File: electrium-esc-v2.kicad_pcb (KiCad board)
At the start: 2 copper layers, 42.3 x 45.4 mm, 65 parts, among them IC1 LMR36510FADDAR, J1 CAN, J2 Conn_01x02, J3 USB_B_Micro, J4 Debugger Pins, J5 GPIO, U1 W25Q128JVS, U2 NCP1117-3.3_SOT223, U3 RP2040, U4 DRV8323HRTAR, U5 NRF24L01_Breakout, U6 SN65HVD233, Y1 ABLS-12.000MHZ-B4-T

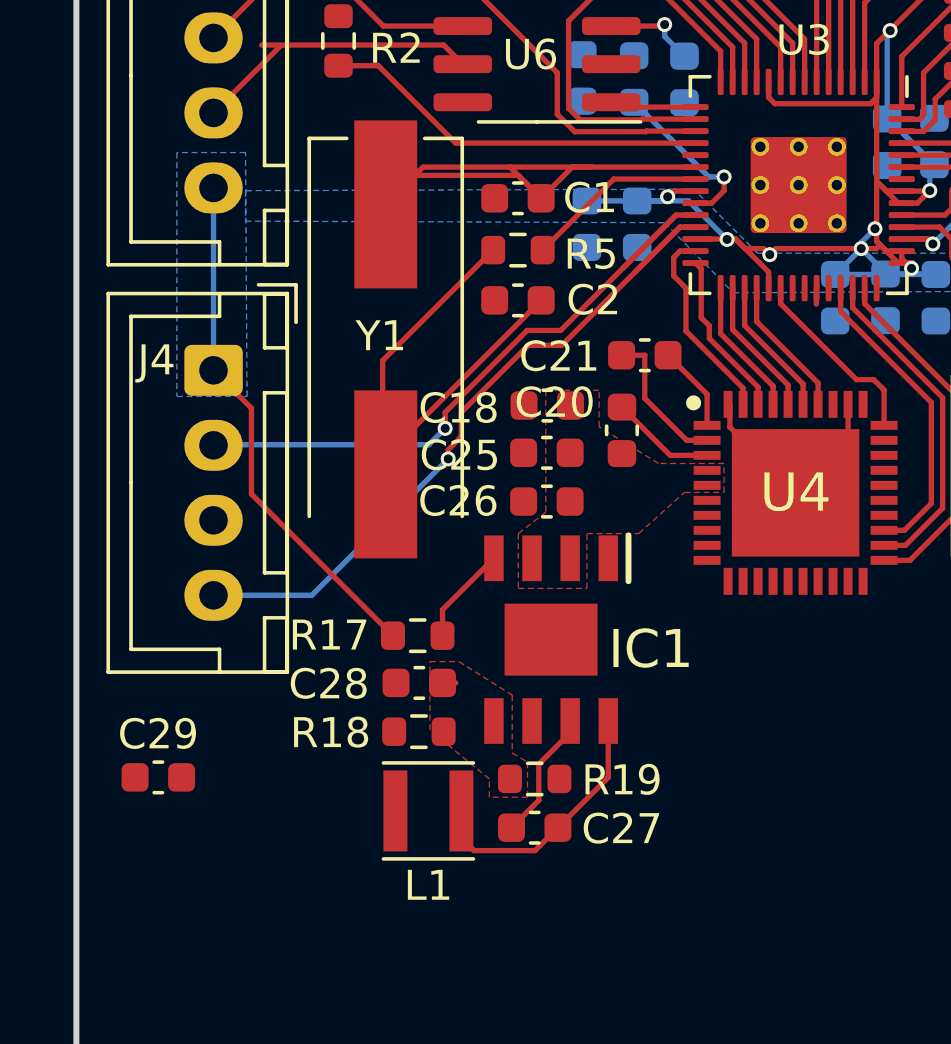
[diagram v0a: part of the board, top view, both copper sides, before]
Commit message: Add proper footprints
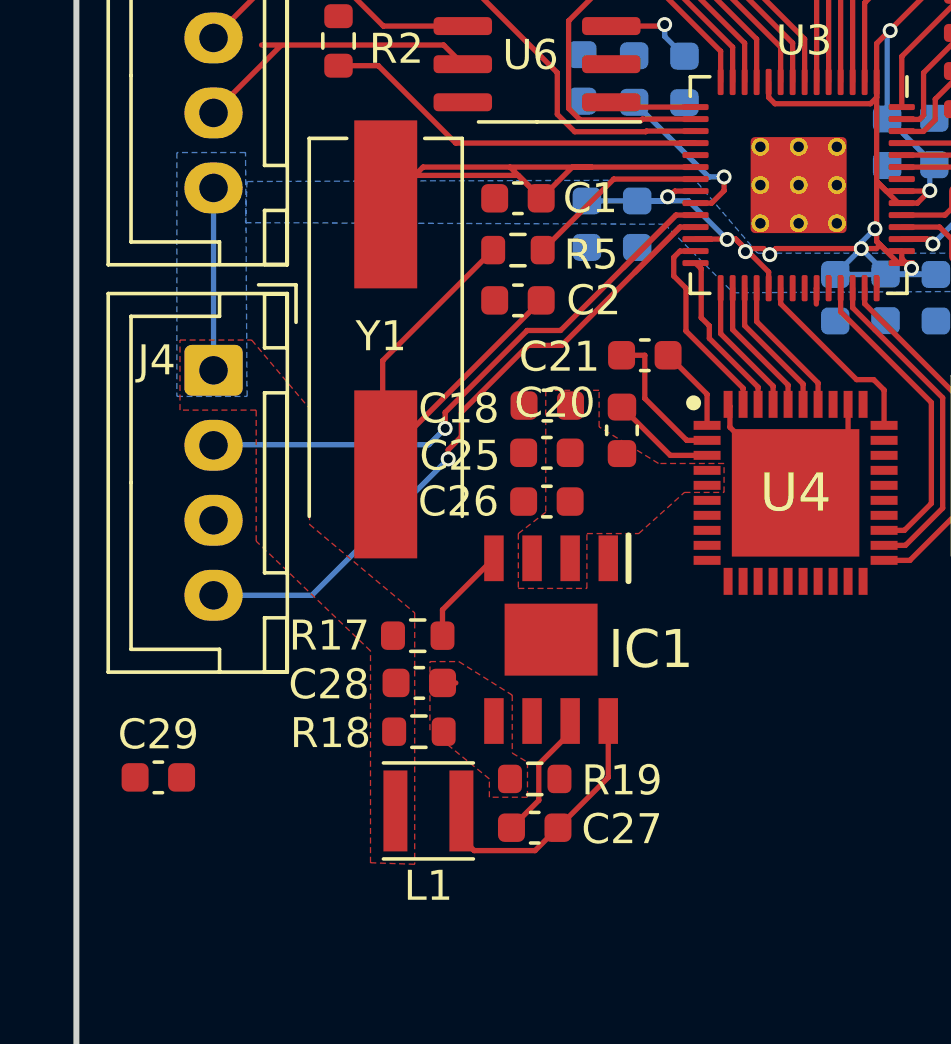
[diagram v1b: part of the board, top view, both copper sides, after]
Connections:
- R2 pad 2: /MCU (RP2040)/LED -> (no net)
- U5 pad 3: /MCU (RP2040)/NRF_CE -> (no net)
- U5 pad 4: /MCU (RP2040)/NRF_CS -> (no net)
- U5 pad 5: /MCU (RP2040)/NRF_CLK -> (no net)
- U5 pad 6: /MCU (RP2040)/NRF_MOSI -> (no net)
- U5 pad 7: /MCU (RP2040)/NRF_MISO -> (no net)
- U6 pad 1: /MCU (RP2040)/CANTX -> (no net)
- U6 pad 4: /MCU (RP2040)/CANRX -> (no net)
- U6 pad 5: /MCU (RP2040)/LBK -> (no net)
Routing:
- net +3.3V: track 105.5 -> 94.3 mm, vias 10 -> 11
- added copper zone on F.Cu, net +3.3V
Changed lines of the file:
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@@
       (net 15 "Net-(D2-A)") (pintype "passive"))
     (pad "2" smd roundrect (at 0.825 0 270) (size 0.8 0.95) (layers "F.Cu" "F.Paste" "F.Mask") (roundrect_rratio 0.25)
-      (net 33 "/MCU (RP2040)/LED") (pintype "passive"))
+      (pintype "passive"))
     (model "${KICAD6_3DMODEL_DIR}/Resistor_SMD.3dshapes/R_0603_1608Metric.wrl"
       (offset (xyz 0 0 0))
@@
       (net 5 "+3.3V") (pinfunction "VCC") (pintype "power_in"))
     (pad "3" thru_hole circle (at 0 2.54 90) (size 1.7 1.7) (drill 1) (layers "*.Cu" "*.Mask")
-      (net 53 "/MCU (RP2040)/NRF_CE") (pinfunction "CE") (pintype "input"))
+      (pinfunction "CE") (pintype "input"))
     (pad "4" thru_hole circle (at 2.54 2.54 90) (size 1.7 1.7) (drill 1) (layers "*.Cu" "*.Mask")
-      (net 50 "/MCU (RP2040)/NRF_CS") (pinfunction "~{CSN}") (pintype "input"))
+      (pinfunction "~{CSN}") (pintype "input"))
     (pad "5" thru_hole circle (at 0 5.08 90) (size 1.7 1.7) (drill 1) (layers "*.Cu" "*.Mask")
-      (net 51 "/MCU (RP2040)/NRF_CLK") (pinfunction "SCK") (pintype "input"))
+      (pinfunction "SCK") (pintype "input"))
     (pad "6" thru_hole circle (at 2.54 5.08 90) (size 1.7 1.7) (drill 1) (layers "*.Cu" "*.Mask")
-      (net 52 "/MCU (RP2040)/NRF_MOSI") (pinfunction "MOSI") (pintype "input"))
+      (pinfunction "MOSI") (pintype "input"))
     (pad "7" thru_hole circle (at 0 7.62 90) (size 1.7 1.7) (drill 1) (layers "*.Cu" "*.Mask")
-      (net 49 "/MCU (RP2040)/NRF_MISO") (pinfunction "MISO") (pintype "output"))
+      (pinfunction "MISO") (pintype "output"))
     (pad "8" thru_hole circle (at 2.54 7.62 90) (size 1.7 1.7) (drill 1) (layers "*.Cu" "*.Mask")
       (net 68 "unconnected-(U5-IRQ-Pad8)") (pinfunction "IRQ") (pintype "output+no_connect"))
@@
       (stroke (width 0.1) (type solid)) (layer "F.Fab"))
     (pad "1" smd roundrect (at -2.475 -1.905 180) (size 1.95 0.6) (layers "F.Cu" "F.Paste" "F.Mask") (roundrect_rratio 0.25)
-      (net 54 "/MCU (RP2040)/CANTX") (pinfunction "D") (pintype "input"))
+      (pinfunction "D") (pintype "input"))
     (pad "2" smd roundrect (at -2.475 -0.635 180) (size 1.95 0.6) (layers "F.Cu" "F.Paste" "F.Mask") (roundrect_rratio 0.25)
       (net 2 "GND") (pinfunction "GND") (pintype "power_in"))
@@
       (net 5 "+3.3V") (pinfunction "VCC") (pintype "power_in"))
     (pad "4" smd roundrect (at -2.475 1.905 180) (size 1.95 0.6) (layers "F.Cu" "F.Paste" "F.Mask") (roundrect_rratio 0.25)
-      (net 55 "/MCU (RP2040)/CANRX") (pinfunction "R") (pintype "output"))
+      (pinfunction "R") (pintype "output"))
     (pad "5" smd roundrect (at 2.475 1.905 180) (size 1.95 0.6) (layers "F.Cu" "F.Paste" "F.Mask") (roundrect_rratio 0.25)
-      (net 56 "/MCU (RP2040)/LBK") (pinfunction "LBK") (pintype "input"))
+      (pinfunction "LBK") (pintype "input"))
     (pad "6" smd roundrect (at 2.475 0.635 180) (size 1.95 0.6) (layers "F.Cu" "F.Paste" "F.Mask") (roundrect_rratio 0.25)
       (net 18 "/CAN/CANL") (pinfunction "CANL") (pintype "bidirectional"))
@@
   (segment (start 184.984723 60.2305) (end 184.664 59.909777) (width 0.1778) (layer "F.Cu") (net 5))
   (segment (start 194.906 51.309352) (end 192.041924 48.445276) (width 0.1778) (layer "F.Cu") (net 5))
+  (segment (start 180.2892 60.154223) (end 180.2892 60.2488) (width 0.1778) (layer "F.Cu") (net 5))
   (segment (start 184.779712 60.025488) (end 184.664 59.909777) (width 0.1778) (layer "F.Cu") (net 5))
   (segment (start 184.984723 58.2305) (end 184.664 57.909777) (width 0.1778) (layer "F.Cu") (net 5))
@@
   (segment (start 185.5015 60.2305) (end 184.984723 60.2305) (width 0.1778) (layer "F.Cu") (net 5))
   (segment (start 185.5015 58.2305) (end 184.984723 58.2305) (width 0.1778) (layer "F.Cu") (net 5))
-  (segment (start 179.965477 59.8305) (end 181.064 60.929023) (width 0.1778) (layer "F.Cu") (net 5))
+  (segment (start 179.965477 59.8305) (end 180.2892 60.154223) (width 0.1778) (layer "F.Cu") (net 5))
   (segment (start 184.15 60.1472) (end 184.2008 60.1472) (width 0.1778) (layer "F.Cu") (net 5))
   (segment (start 184.664 55.112) (end 184.664 54.593) (width 0.1778) (layer "F.Cu") (net 5))
   (segment (start 177.546 52.7304) (end 177.5968 52.7812) (width 0.1778) (layer "F.Cu") (net 5))
-  (segment (start 168.5422 73.0504) (end 163.8239 68.3321) (width 0.1778) (layer "F.Cu") (net 5))
   (segment (start 190.6016 69.444) (end 190.6016 67.9196) (width 0.1778) (layer "F.Cu") (net 5))
-  (segment (start 163.8239 68.3321) (end 163.8239 65.4697) (width 0.1778) (layer "F.Cu") (net 5))
+  (segment (start 180.2892 60.2488) (end 180.383777 60.2488) (width 0.1778) (layer "F.Cu") (net 5))
   (segment (start 180.8988 60.1472) (end 181.102 60.3504) (width 0.1778) (layer "F.Cu") (net 5))
   (segment (start 178.6265 58.2305) (end 177.9387 58.2305) (width 0.1778) (layer "F.Cu") (net 5))
   (segment (start 188.304748 44.7081) (end 181.3519 44.7081) (width 0.1778) (layer "F.Cu") (net 5))
   (segment (start 175.8188 52.7304) (end 177.546 52.7304) (width 0.1778) (layer "F.Cu") (net 5))
+  (segment (start 180.383777 60.2488) (end 181.064 60.929023) (width 0.1778) (layer "F.Cu") (net 5))
   (segment (start 184.664 59.43) (end 184.664 57.909777) (width 0.1778) (layer "F.Cu") (net 5))
   (segment (start 186.0223 58.6305) (end 186.436 58.2168) (width 0.1778) (layer "F.Cu") (net 5))
   (segment (start 190.3476 63.0932) (end 189.0587 61.8043) (width 0.1778) (layer "F.Cu") (net 5))
-  (segment (start 163.8239 65.4697) (end 162.56 64.2058) (width 0.1778) (layer "F.Cu") (net 5))
   (segment (start 181.064 55.109777) (end 181.273623 55.3194) (width 0.1778) (layer "F.Cu") (net 5))
   (segment (start 184.4566 55.3194) (end 184.664 55.112) (width 0.1778) (layer "F.Cu") (net 5))
@@
   (via (at 181.102 60.3504) (size 0.5) (drill 0.3) (layers "F.Cu" "B.Cu") (net 5))
   (via (at 185.8264 60.8076) (size 0.5) (drill 0.3) (layers "F.Cu" "B.Cu") (net 5))
+  (via (at 180.2892 60.2488) (size 0.5) (drill 0.3) (layers "F.Cu" "B.Cu") (net 5))
   (via (at 179.6796 59.8424) (size 0.5) (drill 0.3) (layers "F.Cu" "B.Cu") (net 5))
   (via (at 177.6984 58.42) (size 0.5) (drill 0.3) (layers "F.Cu" "B.Cu") (net 5))
@@
     )
   )
+  (zone (net 5) (net_name "+3.3V") (layer "F.Cu") (hatch edge 0.5)
+    (priority 4)
+    (connect_pads yes (clearance 0.25))
+    (min_thickness 0.25) (filled_areas_thickness no)
+    (fill yes (thermal_gap 0.5) (thermal_bridge_width 0.5))
+    (polygon
+      (pts
+        (xy 169.2656 72.2884)
+        (xy 169.2656 80.6704)
+        (xy 167.7924 80.6196)
+        (xy 167.7924 73.5584)
+        (xy 163.9824 69.9008)
+        (xy 163.9824 65.532)
+        (xy 161.4424 65.532)
+        (xy 161.4424 63.1952)
+        (xy 163.83 63.1952)
+        (xy 165.7604 65.4812)
+        (xy 165.7604 69.342)
+      )
+    )
+  )
   (zone (net 7) (net_name "PWR_SRC") (layer "F.Cu") (name "pwr") (hatch edge 0.5)
     (priority 1)
@@
     (polygon
       (pts
-        (xy 163.6268 59.2328)
-        (xy 177.5968 59.2836)
+        (xy 163.6268 59.2836)
+        (xy 177.5968 59.3344)
         (xy 179.8828 61.6204)
         (xy 188.8236 61.5696)
         (xy 188.8744 60.2996)
         (xy 180.6956 60.2996)
-        (xy 178.562 58.166)
-        (xy 163.6268 58.2168)
+        (xy 178.6128 57.8612)
+        (xy 163.6776 57.912)
       )
     )

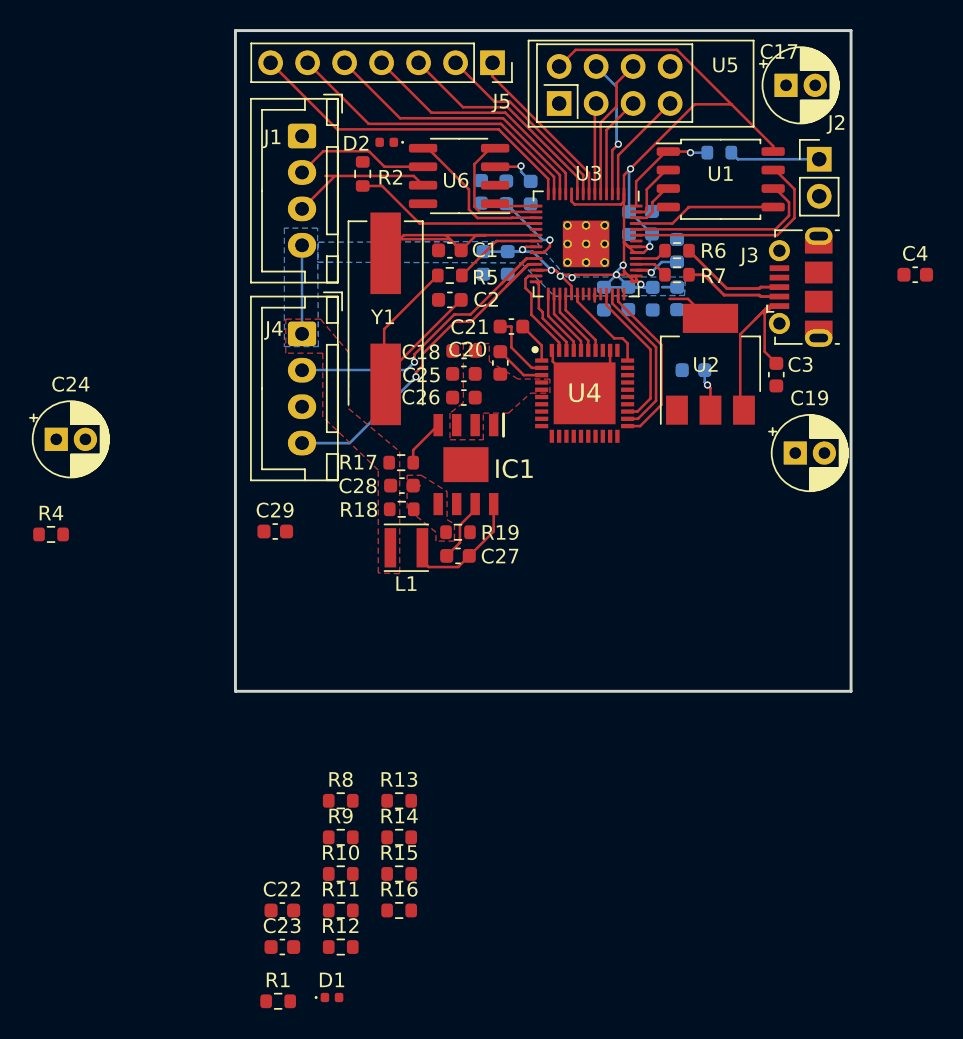
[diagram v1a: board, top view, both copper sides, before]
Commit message: Final schematic with no DRC errors
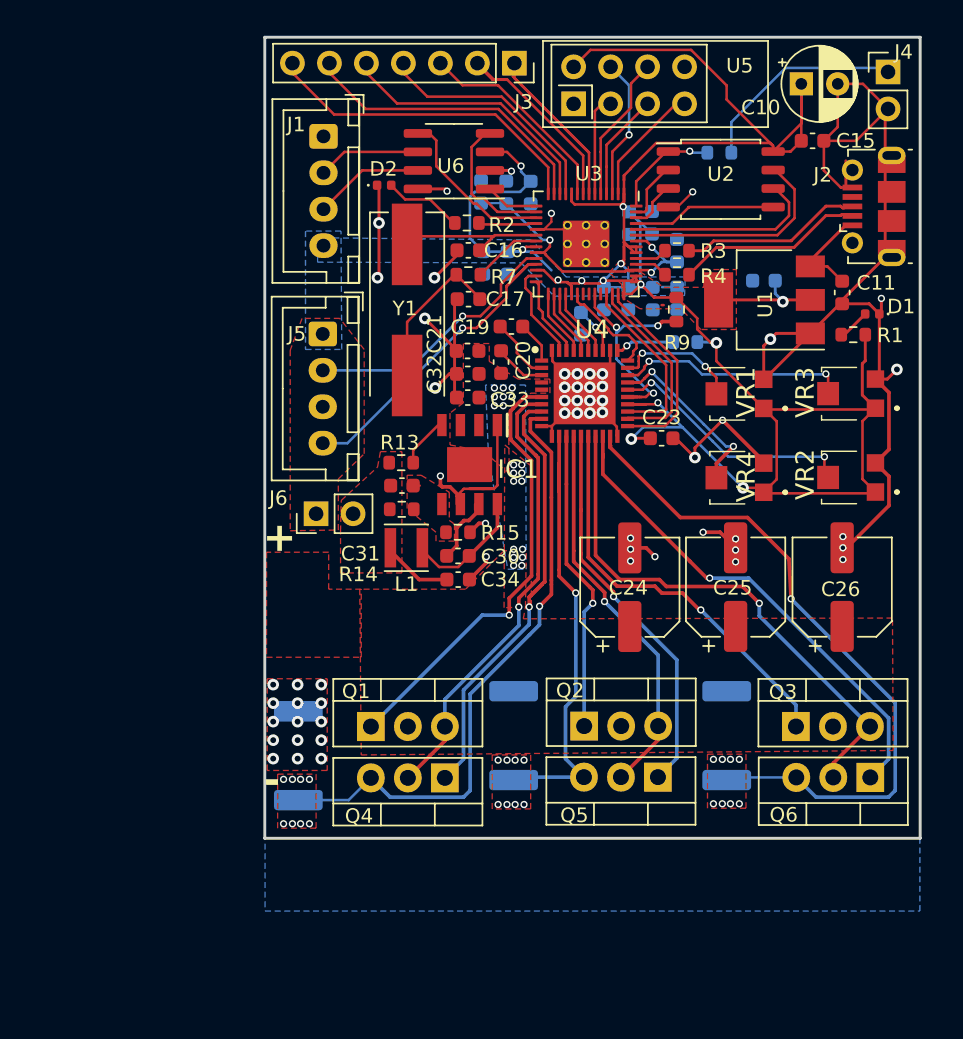
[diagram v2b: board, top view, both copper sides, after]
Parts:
- removed the C19 at (196.4, 72.4)
- removed C22: 1u, Capacitor_SMD:C_0603_1608Metric
- removed the R13 at (169.2, 96.3)
- removed the R14 at (169.2, 98.8)
- removed the R15 at (169.2, 101.3)
- removed R16: 47k, Resistor_SMD:R_0603_1608Metric
- removed the R4 at (145.3, 78.0)
- added C18: 1u, Capacitor_SMD:C_0603_1608Metric, B.Cu at (181.7, 63.5)
- added C25: 22u, Capacitor_SMD:CP_Elec_6.3x7.7, F.Cu at (192.3, 81.6)
- added C26: 22u, Capacitor_SMD:CP_Elec_6.3x7.7, F.Cu at (199.6, 81.6)
- added J6: 3.3VJumper, Connector_PinHeader_2.54mm:PinHeader_1x02_P2.54mm_Vertical, F.Cu at (163.5, 76.6)
- added Q1: IRF3205, Package_TO_SOT_THT:TO-220-3_Vertical, F.Cu at (167.3, 91.2)
- added Q2: IRF3205, Package_TO_SOT_THT:TO-220-3_Vertical, F.Cu at (181.9, 91.1)
- added Q3: IRF3205, Package_TO_SOT_THT:TO-220-3_Vertical, F.Cu at (196.5, 91.2)
- added Q4: IRF3205, Package_TO_SOT_THT:TO-220-3_Vertical, F.Cu at (172.4, 94.7)
- added Q5: IRF3205, Package_TO_SOT_THT:TO-220-3_Vertical, F.Cu at (187.0, 94.6)
- added Q6: IRF3205, Package_TO_SOT_THT:TO-220-3_Vertical, F.Cu at (201.6, 94.7)
- added VR1: VG039NCHXTB204, VG039NCHXTB204:VG039NCHXTB204, F.Cu at (192.5, 68.3)
- added VR2: VG039NCHXTB204, VG039NCHXTB204:VG039NCHXTB204, F.Cu at (200.1, 74.1)
- added VR3: VG039NCHXTB204, VG039NCHXTB204:VG039NCHXTB204, F.Cu at (200.1, 68.3)
- added VR4: VG039NCHXTB204, VG039NCHXTB204:VG039NCHXTB204, F.Cu at (192.5, 74.1)
- C10: renamed from C17; footprint Capacitor_THT:CP_Radial_D5.0mm_P2.00mm -> Capacitor_THT:CP_Radial_D5.0mm_P2.50mm
- C24: value 47u -> 22u; footprint Capacitor_THT:CP_Radial_D5.0mm_P2.00mm -> Capacitor_SMD:CP_Elec_6.3x7.7
- R10: value 10k -> .01; footprint Resistor_SMD:R_0603_1608Metric -> Resistor_SMD:R_2512_6332Metric_Pad1.40x3.35mm_HandSolder; moved to B.Cu
- R11, R12: value 75k -> .01; footprint Resistor_SMD:R_0603_1608Metric -> Resistor_SMD:R_2512_6332Metric_Pad1.40x3.35mm_HandSolder; moved to B.Cu
- R8: moved to B.Cu
- moved R1 60.4 mm to (200.4, 64.3)
- moved D1 59.8 mm to (201.7, 62.8), turned to 180 degrees
- moved C23 43.6 mm to (187.2, 71.4)
- moved R9 42.9 mm to (188.3, 62.5), turned to -90 degrees
- moved C24 40.7 mm to (185.1, 81.6), turned to 90 degrees
- moved R8 39.4 mm to (188.9, 64.8)
- moved R12 30.2 mm to (191.7, 91.8), turned to 90 degrees
- moved R11 16.9 mm to (177.1, 91.8), turned to 90 degrees
- moved C34 13.0 mm to (173.3, 81.1), turned to 180 degrees
- moved C15 11.6 mm to (197.6, 51.0)
- moved R10 8.62 mm to (162.3, 93.2), turned to 90 degrees
- moved R2 7.90 mm to (173.9, 56.6), turned to 0 degrees
- moved C12 7.82 mm to (194.3, 60.6)
- moved J4 7.63 mm to (202.8, 46.2)
- moved J2 7.47 mm to (201.8, 55.5)
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- renumbered C6 to C1, C3 to C11, C5 to C12, C8 to C13, C10 to C14, C4 to C15, C1 to C16, C2 to C17, C21 to C19, C7 to C2, C18 to C21, C9 to C3, C27 to C30, C28 to C31, C25 to C32, C26 to C33, C29 to C34, C30 to C35, C11 to C4, C12 to C5, C13 to C6, C14 to C7, C15 to C8, C16 to C9, J3 to J2, J5 to J3, J2 to J4, J4 to J5, R17 to R13, R18 to R14, R19 to R15, R6 to R3, R7 to R4, R3 to R6, R5 to R7, U2 to U1, U1 to U2
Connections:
- net /Buck Converter (LMR36510FADDAR)/FB renamed Net-(IC1-FB)
- net /MCU (RP2040)/ENABLE renamed /MCU/ENABLE
- net /MCU (RP2040)/OUT_H1 renamed /MCU/OUT_H1
- net /MCU (RP2040)/OUT_H2 renamed /MCU/OUT_H2
- net /MCU (RP2040)/OUT_H3 renamed /MCU/OUT_H3
- net /MCU (RP2040)/OUT_L1 renamed /MCU/OUT_L1
- net /MCU (RP2040)/OUT_L2 renamed /MCU/OUT_L2
- net /MCU (RP2040)/OUT_L3 renamed /MCU/OUT_L3
- net /MCU (RP2040)/QSPI_SCLK renamed /MCU/QSPI_SCLK
- net /MCU (RP2040)/QSPI_SD0 renamed /MCU/QSPI_SD0
- net /MCU (RP2040)/QSPI_SD1 renamed /MCU/QSPI_SD1
- net /MCU (RP2040)/QSPI_SD2 renamed /MCU/QSPI_SD2
- net /MCU (RP2040)/QSPI_SD3 renamed /MCU/QSPI_SD3
- net /MCU (RP2040)/QSPI_SS renamed /MCU/QSPI_SS
- net /MCU (RP2040)/SENS1 renamed /MCU/SENS1
- net /MCU (RP2040)/SENS2 renamed /MCU/SENS2
- net /MCU (RP2040)/SENS3 renamed /MCU/SENS3
- net /MCU (RP2040)/SWCLK renamed /MCU/SWCLK
- net /MCU (RP2040)/SWD renamed /MCU/SWD
- net /MCU (RP2040)/USB_D+ renamed /MCU/USB_D+
- net /MCU (RP2040)/USB_D- renamed /MCU/USB_D-
- net /MCU (RP2040)/XIN renamed /MCU/XIN
- net /MCU (RP2040)/XOUT renamed /MCU/XOUT
- net /MCU (RP2040)/~{USB_BOOT} renamed /MCU/~{USB_BOOT}
- C24 pad 1: +3.3V -> PWR_SRC
- C31 pad 2: +3.3V -> /Buck Converter (LMR160006XDDCR)/LMR_OUT
- C34 pad 2: +3.3V -> /Buck Converter (LMR160006XDDCR)/LMR_OUT
- L1 pad 2: +3.3V -> /Buck Converter (LMR160006XDDCR)/LMR_OUT
- R10 pad 1: /MCU (RP2040)/MODE -> /MOSFETs/SP1
- R11 pad 1: +3.3V -> /MOSFETs/SP2
- R11 pad 2: /MCU (RP2040)/IDRIVE -> GND
- R12 pad 1: /MCU (RP2040)/IDRIVE -> /MOSFETs/SP3
- R13 pad 2: +3.3V -> /Buck Converter (LMR160006XDDCR)/LMR_OUT
- R14 pad 1: +3.3V -> /Buck Converter (LMR160006XDDCR)/LMR_OUT
- R2 pad 2: (no net) -> /MCU/LED
- R9 pad 1: /MCU (RP2040)/NFAULT -> +3.3V
- R9 pad 2: +3.3V -> /MCU/NFAULT
- U3 pad 15: /MCU (RP2040)/CANTX -> /MCU/CANTX
- U3 pad 16: /MCU (RP2040)/CANRX -> /MCU/CANRX
- U3 pad 17: /MCU (RP2040)/LBK -> /MCU/LBK
- U3 pad 18: /MCU (RP2040)/LED -> /MCU/LED
- U3 pad 2: /MCU (RP2040)/NRF_MISO -> /MCU/NRF_MISO
- U3 pad 3: /MCU (RP2040)/NRF_CS -> /MCU/NRF_CSN
- U3 pad 35: /MCU (RP2040)/IDRIVE -> unconnected-(U3-GPIO23-Pad35)
- U3 pad 36: /MCU (RP2040)/MODE -> unconnected-(U3-GPIO24-Pad36)
- U3 pad 37: /MCU (RP2040)/NFAULT -> /MCU/NFAULT
- U3 pad 4: /MCU (RP2040)/NRF_CLK -> /MCU/NRF_SCLK
- U3 pad 5: /MCU (RP2040)/NRF_MOSI -> /MCU/NRF_MOSI
- U3 pad 6: /MCU (RP2040)/NRF_CE -> /MCU/NRF_CE
- U4 pad 10: /Motor Driver (DRV8323)/SN1 -> GND
- U4 pad 11: /Motor Driver (DRV8323)/SN2 -> GND
- U4 pad 12: /Motor Driver (DRV8323)/SP2 -> /MOSFETs/SP2
- U4 pad 13: /Motor Driver (DRV8323)/M_L2 -> /MOSFETs/M_L2
- U4 pad 14: /Motor Driver (DRV8323)/SH2 -> /MOSFETs/SH2
- U4 pad 15: /Motor Driver (DRV8323)/M_H2 -> /MOSFETs/M_H2
- U4 pad 16: /Motor Driver (DRV8323)/M_H3 -> /MOSFETs/M_H3
- U4 pad 17: /Motor Driver (DRV8323)/SH3 -> /MOSFETs/SH3
- U4 pad 18: /Motor Driver (DRV8323)/M_L3 -> /MOSFETs/M_L3
- U4 pad 19: /Motor Driver (DRV8323)/SP3 -> /MOSFETs/SP3
- U4 pad 20: /Motor Driver (DRV8323)/SN3 -> GND
- U4 pad 25: /MCU (RP2040)/NFAULT -> /MCU/NFAULT
- U4 pad 26: /MCU (RP2040)/MODE -> MODE
- U4 pad 27: /MCU (RP2040)/IDRIVE -> IDRIVE
- U4 pad 28: Net-(U4-VDS) -> VDS
- U4 pad 29: Net-(U4-GAIN) -> GAIN
- U4 pad 6: /Motor Driver (DRV8323)/M_H1 -> /MOSFETs/M_H1
- U4 pad 7: /Motor Driver (DRV8323)/SH1 -> /MOSFETs/SH1
- U4 pad 8: /Motor Driver (DRV8323)/M_L1 -> /MOSFETs/M_L1
- U4 pad 9: /Motor Driver (DRV8323)/SP1 -> /MOSFETs/SP1
- U5 pad 3: (no net) -> /MCU/NRF_CE
- U5 pad 4: (no net) -> /MCU/NRF_CSN
- U5 pad 5: (no net) -> /MCU/NRF_SCLK
- U5 pad 6: (no net) -> /MCU/NRF_MOSI
- U5 pad 7: (no net) -> /MCU/NRF_MISO
- U6 pad 1: (no net) -> /MCU/CANTX
- U6 pad 4: (no net) -> /MCU/CANRX
- U6 pad 5: (no net) -> /MCU/LBK
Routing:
- net GND: track 8.97 -> 149.2 mm, vias 0 -> 83
- net +3.3V: track 94.3 -> 181.7 mm, vias 11 -> 13
- net /MOSFETs/SP3: track 0.00 -> 48.7 mm, vias 0 -> 1
- net /MOSFETs/SP1: track 0.00 -> 42.4 mm, vias 0 -> 1
- net /MOSFETs/SH3: track 0.00 -> 36.9 mm, vias 0 -> 1
- net /MOSFETs/M_L3: track 0.00 -> 34.0 mm, vias 0 -> 1
- net /MOSFETs/SP2: track 0.00 -> 31.7 mm, vias 0 -> 1
- net /MOSFETs/SH1: track 0.00 -> 31.3 mm, vias 0 -> 1
- net /MOSFETs/M_L1: track 0.00 -> 30.8 mm, vias 0 -> 1
- net /MOSFETs/M_H1: track 0.00 -> 30.5 mm, vias 0 -> 1
- net /MOSFETs/M_H3: track 0.00 -> 28.1 mm, vias 0 -> 1
- net /MOSFETs/SH2: track 0.00 -> 26.9 mm, vias 0 -> 1
- net /MOSFETs/M_H2: track 0.00 -> 26.7 mm, vias 0 -> 1
- net /MOSFETs/M_L2: track 0.00 -> 20.9 mm, vias 0 -> 1
- net MODE: track 0.00 -> 17.2 mm, vias 0 -> 2
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- added copper zone on F.Cu, net /Buck Converter (LMR160006XDDCR)/LMR_OUT
- added copper zone on B.Cu, net GND
- added copper zone on F.Cu, net GND
- added copper zone on B.Cu, net PWR_SRC
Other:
- board size 42.3 x 45.4 mm -> 45 x 55 mm
- board text added: "+"
- board text added: "-"
- board text added: "Electrium Mobility ESC V2.0"
